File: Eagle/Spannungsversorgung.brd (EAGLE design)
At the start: 160 x 100 mm, 5 parts, among them U1 ESP32-S2-SAOLA-1R

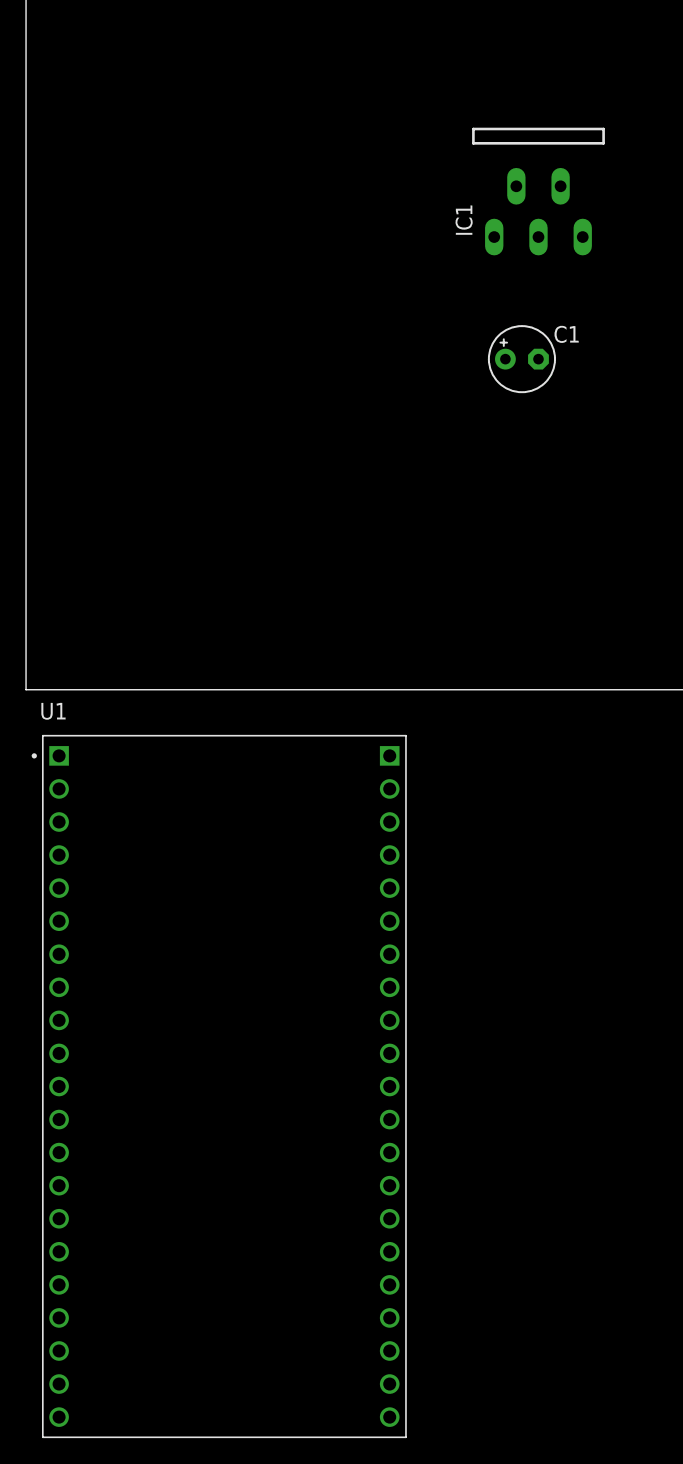
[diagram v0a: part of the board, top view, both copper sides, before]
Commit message: Added Features & Verwendung to the documentation of LT1529-5
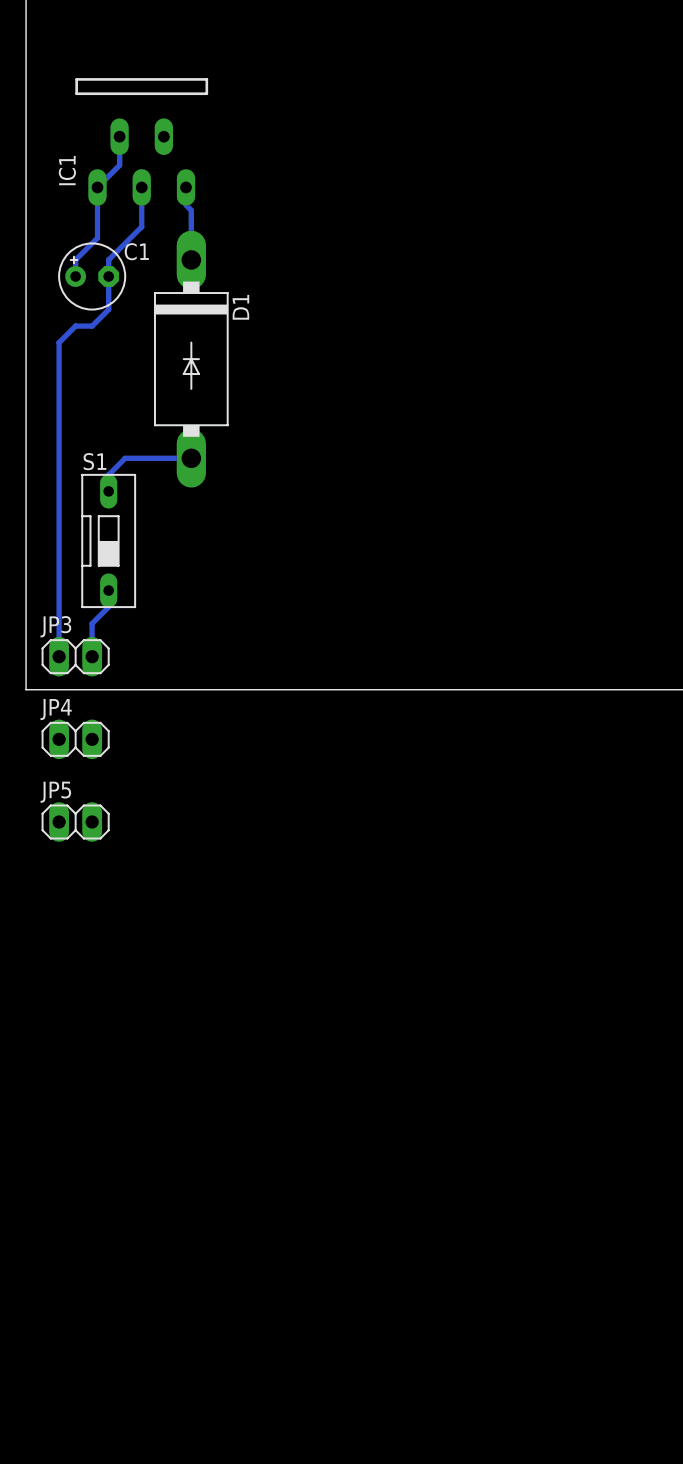
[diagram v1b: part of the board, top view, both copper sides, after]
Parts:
- removed U1: ESP32-S2-SAOLA-1R, ESP32-S2-SAOLA-1R:XCVR_ESP32-S2-SAOLA-1R
- added D1: 1N5400, diode:DO201-15
- added JP3, JP4, JP5: (no value), pinhead:1X02
- added S1: (no value), switch-dil:DS-01
- moved C1 33.6 mm to (5.08, 31.8)
- moved IC1 30.7 mm to (8.89, 47.0)
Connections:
- removed net 3V3: U1.A1
- removed net 5V0: U1.A20
- new net N$2: D1.C, IC1.5
- net BATTERY: now also D1.A, JP3.2, S1.1, S1.2; no longer IC1.5
- net GND: now also JP3.1, JP4.1, JP5.1; no longer U1.A21, U1.B1
- net VOUT: now also JP4.2, JP5.2
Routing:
- net GND: track 0.00 -> 39.4 mm
- net BATTERY: track 0.00 -> 13.8 mm
- net VOUT: track 0.00 -> 12.1 mm
- net N$2: track 0.00 -> 5.74 mm
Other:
- board text added: "1000mil"
